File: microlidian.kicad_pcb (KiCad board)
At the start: 2 copper layers, 128.9 x 128.5 mm, 31 parts, among them J1 Eurorack power, J11 Backboard Conn 1, J12 Frontboard Conn 1, J13 Backboard Conn 2, J14 Frontboard Conn 2, J2 ST7789 TFT socket, J3 Expansion header, J4 ADS1015 digital side, J5 ADS1015 analog side, J7 TRS MIDI Out, SW1 RotaryEncoder_Switch, SW2 Back button, U1 SeeeduinoXIAO, U2 L78L05

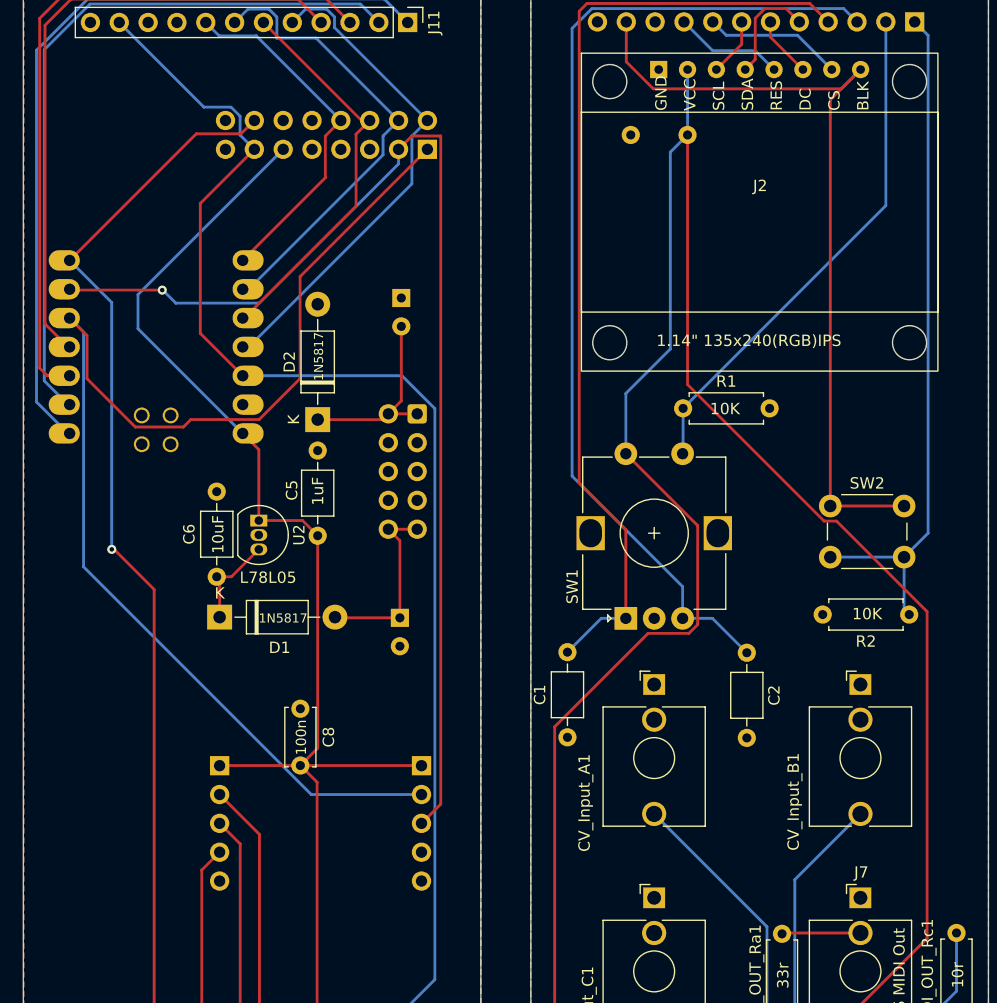
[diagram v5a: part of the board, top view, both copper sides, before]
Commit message: added pullup on RES, think this actually fixes power on screen problem!! :D
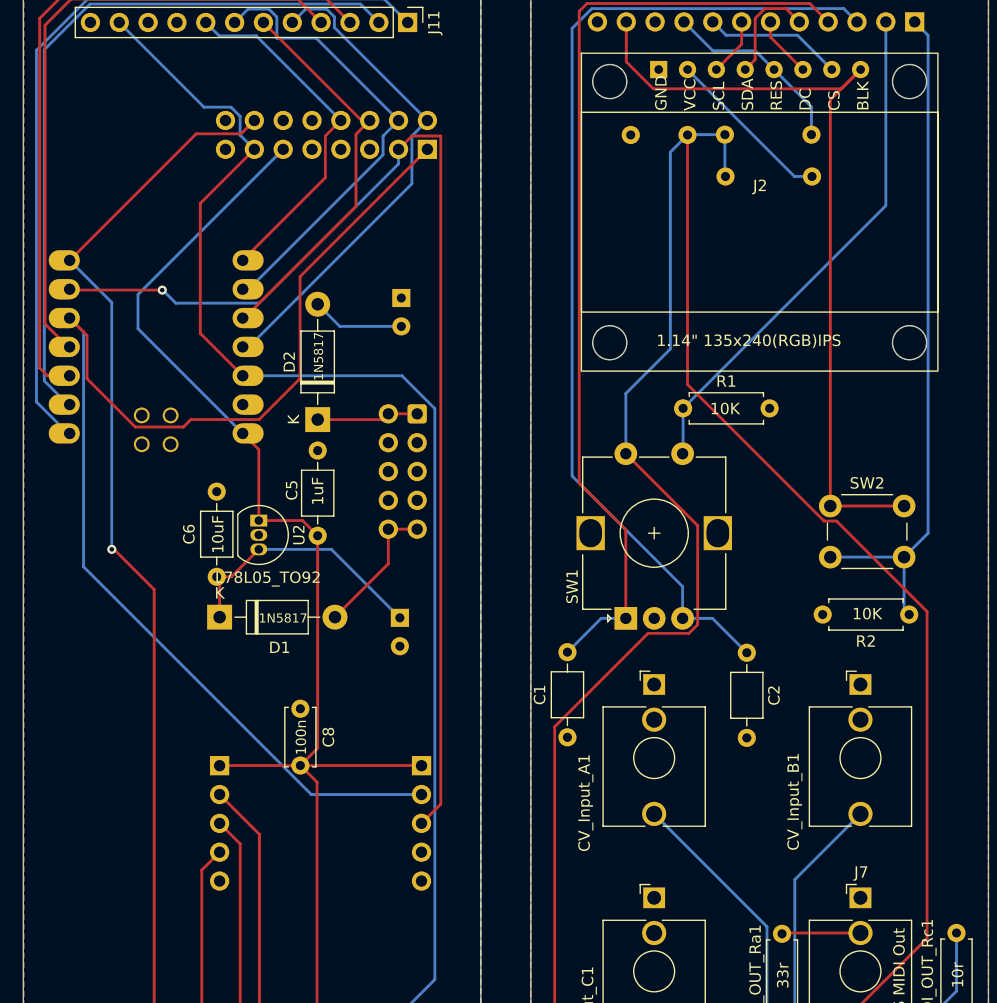
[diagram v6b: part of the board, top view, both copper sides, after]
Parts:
- added R3: 100R, Resistor_THT:R_Axial_DIN0207_L6.3mm_D2.5mm_P7.62mm_Horizontal, B.Cu at (100.1, 62.7)
- added R4: 1K, Resistor_THT:R_Axial_DIN0207_L6.3mm_D2.5mm_P7.62mm_Horizontal, B.Cu at (100.0, 59.1)
- U2: value L78L05 -> L78L05_TO92
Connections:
- C1 pad 1: Backboard GND -> CV GND
- C2 pad 2: Backboard GND -> CV GND
- C3 pad 2: Net-(D2-K) -> -12V
- C4 pad 1: Net-(D1-A) -> +12V
- C7 pad 2: Backboard GND -> CV GND
- CV_Input_A1 pad S: Backboard GND -> CV GND
- CV_Input_A1 pad TN: Backboard GND -> CV GND
- CV_Input_B1 pad S: Backboard GND -> CV GND
- CV_Input_B1 pad TN: Backboard GND -> CV GND
- CV_Input_C1 pad S: Backboard GND -> CV GND
- CV_Input_C1 pad TN: Backboard GND -> CV GND
- J1 pad 4: Backboard GND -> Net-(J1-Pin_4)
- J1 pad 6: Backboard GND -> Net-(J1-Pin_4)
- J1 pad 8: Backboard GND -> Net-(J1-Pin_4)
- J12 pad 12: Backboard GND -> CV GND
- J14 pad 3: Backboard GND -> CV GND
- J14 pad 7: Backboard GND -> CV GND
- J2 pad 1: Backboard GND -> CV GND
- J2 pad 2: Frontboard +3.3V -> Net-(J2-Pin_2)
- J7 pad S: Backboard GND -> CV GND
- R1 pad 2: Backboard GND -> CV GND
- R2 pad 2: Backboard GND -> CV GND
- SW1 pad C: Backboard GND -> CV GND
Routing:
- net Net-(J2-Pin_2): track 0.00 -> 14.9 mm
- net +12V: track 8.36 -> 22.9 mm
- net Net-(D2-K): track 17.1 -> 8.26 mm
- net -12V: track 0.00 -> 8.17 mm
- net TFT reset Frontboard: track 9.67 -> 16.8 mm
- net Net-(D1-A): track 16.5 -> 12.2 mm
- net Frontboard +3.3V: track 226.9 -> 228.1 mm
- net TFT DC Backboard: track 35.1 -> 34.2 mm
- net Back button Frontboard: track 60.2 -> 59.6 mm
- net MOSI Backboard: track 44.0 -> 43.5 mm
- net SPI CLK Backboard: track 40.9 -> 40.4 mm
- added copper zone on B.Cu, net CV GND
- added copper zone on F.Cu, net CV GND

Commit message: fixed connection to ground
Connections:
- J1 pad 4: Net-(J1-Pin_4) -> Backboard GND
- J1 pad 6: Net-(J1-Pin_4) -> Backboard GND
- J1 pad 8: Net-(J1-Pin_4) -> Backboard GND
